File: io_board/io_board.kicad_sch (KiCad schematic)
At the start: 83 parts, among them J10 RST1, J11 D1, J12 Osc2, J13 Rung2, J14 Sin2, J15 Gate2, J16 Ring, J18 RST2, J19 D2, J21 CV1, J22 CV2, J4 STRB1, J5 STRB2, J6 Osc1, J7 Sin1, J8 Rung1, J9 Gate1, Q1 2N3904, Q10 2N3904, Q11 2N3904, Q2 2N3904, Q5 2N3904, Q6 2N3904, Q7 2N3904, Q8 2N3904, Q9 2N3904, SW1 SW_SPDT, U3 TL074

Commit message: Routing done, panel done
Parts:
- U3: value TL074 -> (none); footprint Package_DIP:DIP-14_W7.62mm_Socket_LongPads -> (none)
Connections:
- net Clk2: now also J20.7 (Pin_7); no longer J20.8 (Pin_8)
- net D1: now also J17.5 (Pin_5); no longer J17.4 (Pin_4)
- net Osc1: now also J17.6 (Pin_6); no longer J17.7 (Pin_7)
- net Osc2: now also J20.5 (Pin_5); no longer J20.7 (Pin_7)
- net Osc3sw: now also J20.3 (Pin_3); no longer J20.5 (Pin_5)
- net QB8: now also J20.8 (Pin_8); no longer J20.9 (Pin_9)
- net RM: now also J17.4 (Pin_4); no longer J17.6 (Pin_6)
- net Rst1: now also J17.7 (Pin_7); no longer J17.3 (Pin_3)
- net Rst2: now also J20.9 (Pin_9); no longer J20.3 (Pin_3)
- net Rung2: now also J20.10 (Pin_10); no longer J20.11 (Pin_11)
- net Sin2: now also J20.11 (Pin_11); no longer J20.10 (Pin_10)
- net at R57.1, R59.1: now also U3.12 (+); no longer U3.10 (+)
- net at D9.2 (A): now also U3.14; no longer U3.8
- net at R58.1: now also U3.10 (+); no longer U3.12 (+)
- net at R54.2, R55.1: now also U3.13 (-), U3.9 (-); no longer U3.13 (-), U3.9 (-)
- net at D10.2 (A): now also U3.8; no longer U3.14

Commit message: Updates to panel etc.
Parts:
- added R72, R74: 100k, Resistor_THT:R_Axial_DIN0204_L3.6mm_D1.6mm_P7.62mm_Horizontal, symbol Device:R
- added R73, R75: 22k, Resistor_THT:R_Axial_DIN0204_L3.6mm_D1.6mm_P7.62mm_Horizontal, symbol Device:R
- U3: value (none) -> TL074; footprint (none) -> Package_DIP:DIP-14_W7.62mm_Socket_LongPads
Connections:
- net +12V: now also R72.1, R74.1
- net GND: now also R73.2, R75.2
- net at J22.TN: now also R74.2, R75.1
- net at J21.TN: now also R72.2, R73.1

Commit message: Added negative CV protection diodes
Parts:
- added D13, D14, D15, D16: (no value), symbol Diode:BAT42
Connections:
- net CV1: now also D15.1 (K)
- net CV2: now also D16.1 (K)
- net GND: now also D13.2 (A), D14.2 (A), D15.2 (A), D16.2 (A)
- net at Q8.2 (B), R40.2: now also D14.1 (K)
- net at Q7.2 (B), R39.2: now also D13.1 (K)
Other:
- moved on the sheet: CVR2, FREQ2, J22, R63, R64, R71, R74, R75, TH3, TH4

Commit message: Flip flop on CV protection diodes
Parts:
- removed D15, D16: (no value), symbol Diode:BAT42
- D13, D14: value (none) -> BAT42; footprint (none) -> Diode_THT:D_DO-35_SOD27_P7.62mm_Horizontal
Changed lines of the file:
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@@
   (junction (at 317.5 64.77) (diameter 0) (color 0 0 0 0)
   )
-  (junction (at 323.85 64.77) (diameter 0) (color 0 0 0 0)
-  )
   (junction (at 387.35 64.77) (diameter 0) (color 0 0 0 0)
   )
@@
   (junction (at 125.73 43.18) (diameter 0) (color 0 0 0 0)
   )
-  (junction (at 393.065 64.77) (diameter 0) (color 0 0 0 0)
-  )
   (junction (at 219.71 43.18) (diameter 0) (color 0 0 0 0)
   )
@@
     (stroke (width 0) (type default) (color 0 0 0 0))
   )
-  (wire (pts (xy 323.85 64.77) (xy 327.66 64.77))
-    (stroke (width 0) (type default) (color 0 0 0 0))
-  )
   (polyline (pts (xy 15.24 251.46) (xy 15.24 157.48))
     (stroke (width 0) (type default) (color 0 0 0 0))
@@
     (stroke (width 0) (type default) (color 0 0 0 0))
   )
-  (wire (pts (xy 393.065 64.77) (xy 396.24 64.77))
-    (stroke (width 0) (type default) (color 0 0 0 0))
-  )
   (wire (pts (xy 76.2 138.43) (xy 76.2 139.7))
     (stroke (width 0) (type default) (color 0 0 0 0))
@@
     (stroke (width 0) (type default) (color 0 0 0 0))
   )
-  (wire (pts (xy 323.85 64.77) (xy 323.85 67.945))
-    (stroke (width 0) (type default) (color 0 0 0 0))
-  )
   (wire (pts (xy 167.64 201.93) (xy 170.18 201.93))
     (stroke (width 0) (type default) (color 0 0 0 0))
@@
     (stroke (width 0) (type default) (color 0 0 0 0))
   )
-  (wire (pts (xy 393.065 64.77) (xy 393.065 67.945))
-    (stroke (width 0) (type default) (color 0 0 0 0))
-  )
   (wire (pts (xy 110.49 231.14) (xy 110.49 232.41))
     (stroke (width 0) (type default) (color 0 0 0 0))
@@
     (stroke (width 0) (type default) (color 0 0 0 0))
   )
-  (wire (pts (xy 317.5 64.77) (xy 323.85 64.77))
+  (wire (pts (xy 317.5 64.77) (xy 327.66 64.77))
     (stroke (width 0) (type default) (color 0 0 0 0))
   )
@@
     (stroke (width 0) (type default) (color 0 0 0 0))
   )
-  (wire (pts (xy 393.065 75.565) (xy 393.065 79.375))
-    (stroke (width 0) (type default) (color 0 0 0 0))
-  )
   (wire (pts (xy 40.64 240.03) (xy 40.64 242.57))
     (stroke (width 0) (type default) (color 0 0 0 0))
@@
     (stroke (width 0) (type default) (color 0 0 0 0))
   )
-  (wire (pts (xy 323.85 75.565) (xy 323.85 79.375))
-    (stroke (width 0) (type default) (color 0 0 0 0))
-  )
   (wire (pts (xy 135.89 67.31) (xy 135.89 48.26))
     (stroke (width 0) (type default) (color 0 0 0 0))
@@
     (stroke (width 0) (type default) (color 0 0 0 0))
   )
-  (wire (pts (xy 387.35 64.77) (xy 393.065 64.77))
+  (wire (pts (xy 387.35 64.77) (xy 396.24 64.77))
     (stroke (width 0) (type default) (color 0 0 0 0))
   )
@@
       (effects (font (size 1.27 1.27)) hide)
     )
-    (property "Value" "" (id 1) (at 46.99 104.14 0))
+    (property "Value" "GND" (id 1) (at 46.99 104.14 0))
     (property "Footprint" "" (id 2) (at 46.99 99.06 0)
       (effects (font (size 1.27 1.27)) hide)
@@
       (effects (font (size 1.27 1.27)) (justify left))
     )
-    (property "Value" "" (id 1) (at 39.37 95.25 90)
+    (property "Value" "BAT42" (id 1) (at 39.37 95.25 90)
       (effects (font (size 1.27 1.27)) (justify left))
     )
-    (property "Footprint" "" (id 2) (at 42.545 93.98 0)
+    (property "Footprint" "Diode_THT:D_DO-35_SOD27_P7.62mm_Horizontal" (id 2) (at 42.545 93.98 0)
       (effects (font (size 1.27 1.27)) hide)
     )
@@
       (effects (font (size 1.27 1.27)) hide)
     )
-    (property "Value" "" (id 1) (at 46.99 64.77 0))
+    (property "Value" "GND" (id 1) (at 46.99 64.77 0))
     (property "Footprint" "" (id 2) (at 46.99 59.69 0)
       (effects (font (size 1.27 1.27)) hide)
@@
     (pin "TN")
   )
-  (symbol (lib_id "power:GND") (at 393.065 79.375 0) (unit 1)
-    (in_bom yes) (on_board yes) (fields_autoplaced)
-    (property "Reference" "#PWR097" (id 0) (at 393.065 85.725 0)
-      (effects (font (size 1.27 1.27)) hide)
-    )
-    (property "Value" "" (id 1) (at 393.065 84.455 0))
-    (property "Footprint" "" (id 2) (at 393.065 79.375 0)
-      (effects (font (size 1.27 1.27)) hide)
-    )
-    (property "Datasheet" "" (id 3) (at 393.065 79.375 0)
-      (effects (font (size 1.27 1.27)) hide)
-    )
-    (pin "1")
-  )
   (symbol (lib_id "power:-12V") (at 177.8 156.21 180) (unit 1)
     (in_bom yes) (on_board yes) (fields_autoplaced)
@@
     (pin "3")
   )
-  (symbol (lib_id "Diode:BAT42") (at 393.065 71.755 270) (unit 1)
-    (in_bom yes) (on_board yes) (fields_autoplaced)
-    (property "Reference" "D16" (id 0) (at 395.605 70.1674 90)
-      (effects (font (size 1.27 1.27)) (justify left))
-    )
-    (property "Value" "" (id 1) (at 395.605 72.7074 90)
-      (effects (font (size 1.27 1.27)) (justify left))
-    )
-    (property "Footprint" "" (id 2) (at 388.62 71.755 0)
-      (effects (font (size 1.27 1.27)) hide)
-    )
-    (property "Datasheet" "http://www.vishay.com/docs/85660/bat42.pdf" (id 3) (at 393.065 71.755 0)
-      (effects (font (size 1.27 1.27)) hide)
-    )
-    (pin "1")
-    (pin "2")
-  )
   (symbol (lib_id "Device:R") (at 212.09 201.93 270) (unit 1)
     (in_bom yes) (on_board yes) (fields_autoplaced)
@@
     (pin "2")
   )
-  (symbol (lib_id "Diode:BAT42") (at 323.85 71.755 270) (unit 1)
-    (in_bom yes) (on_board yes) (fields_autoplaced)
-    (property "Reference" "D15" (id 0) (at 326.39 70.1674 90)
-      (effects (font (size 1.27 1.27)) (justify left))
-    )
-    (property "Value" "" (id 1) (at 326.39 72.7074 90)
-      (effects (font (size 1.27 1.27)) (justify left))
-    )
-    (property "Footprint" "" (id 2) (at 319.405 71.755 0)
-      (effects (font (size 1.27 1.27)) hide)
-    )
-    (property "Datasheet" "http://www.vishay.com/docs/85660/bat42.pdf" (id 3) (at 323.85 71.755 0)
-      (effects (font (size 1.27 1.27)) hide)
-    )
-    (pin "1")
-    (pin "2")
-  )
   (symbol (lib_id "Device:R") (at 55.88 54.61 180) (unit 1)
     (in_bom yes) (on_board yes) (fields_autoplaced)
@@
     (pin "2")
   )
-  (symbol (lib_id "power:GND") (at 323.85 79.375 0) (unit 1)
-    (in_bom yes) (on_board yes) (fields_autoplaced)
-    (property "Reference" "#PWR093" (id 0) (at 323.85 85.725 0)
-      (effects (font (size 1.27 1.27)) hide)
-    )
-    (property "Value" "" (id 1) (at 323.85 84.455 0))
-    (property "Footprint" "" (id 2) (at 323.85 79.375 0)
-      (effects (font (size 1.27 1.27)) hide)
-    )
-    (property "Datasheet" "" (id 3) (at 323.85 79.375 0)
-      (effects (font (size 1.27 1.27)) hide)
-    )
-    (pin "1")
-  )
   (symbol (lib_id "Device:R") (at 36.83 196.85 90) (unit 1)
     (in_bom yes) (on_board yes)
@@
       (effects (font (size 1.27 1.27)) (justify left))
     )
-    (property "Value" "" (id 1) (at 39.37 55.88 90)
+    (property "Value" "BAT42" (id 1) (at 39.37 55.88 90)
       (effects (font (size 1.27 1.27)) (justify left))
     )
-    (property "Footprint" "" (id 2) (at 42.545 54.61 0)
+    (property "Footprint" "Diode_THT:D_DO-35_SOD27_P7.62mm_Horizontal" (id 2) (at 42.545 54.61 0)
       (effects (font (size 1.27 1.27)) hide)
     )
@@
       (reference "#PWR092") (unit 1) (value "GND") (footprint "")
     )
-    (path "/c6c801eb-a62e-4709-ba8f-cc4ab2962bb0"
-      (reference "#PWR093") (unit 1) (value "GND") (footprint "")
-    )
-    (path "/5b01a551-5830-4c34-991f-8c4bd9fdd15c"
-      (reference "#PWR097") (unit 1) (value "GND") (footprint "")
-    )
     (path "/5e4d8429-e4c9-42f2-9cfd-97a2e6b0fe00"
       (reference "#PWR0101") (unit 1) (value "GND") (footprint "")
@@
       (reference "D14") (unit 1) (value "BAT42") (footprint "Diode_THT:D_DO-35_SOD27_P7.62mm_Horizontal")
     )
-    (path "/b4e0d83a-1e44-4055-b69b-34a66bed64e8"
-      (reference "D15") (unit 1) (value "BAT42") (footprint "Diode_THT:D_DO-35_SOD27_P7.62mm_Horizontal")
-    )
-    (path "/61cd796f-f9d1-45f6-922e-b46b67f716a1"
-      (reference "D16") (unit 1) (value "BAT42") (footprint "Diode_THT:D_DO-35_SOD27_P7.62mm_Horizontal")
-    )
     (path "/a2167960-f9c9-4609-b610-0da799bcc1d1"

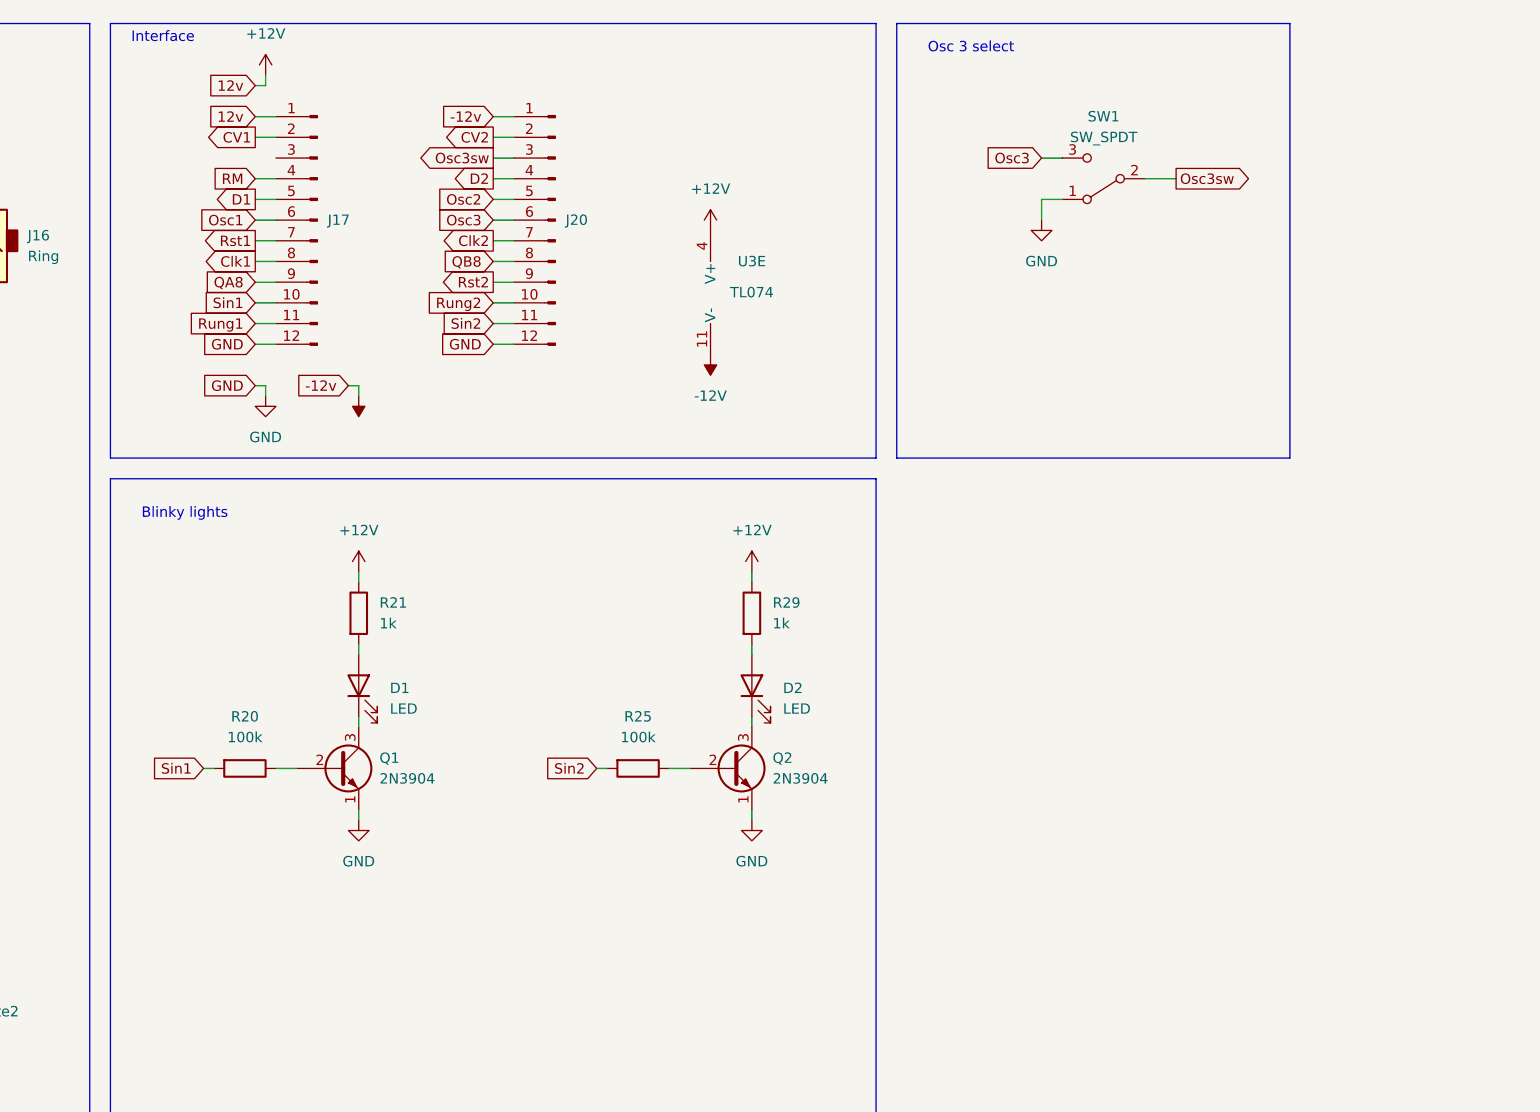
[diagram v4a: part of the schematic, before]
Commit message: Added range switch
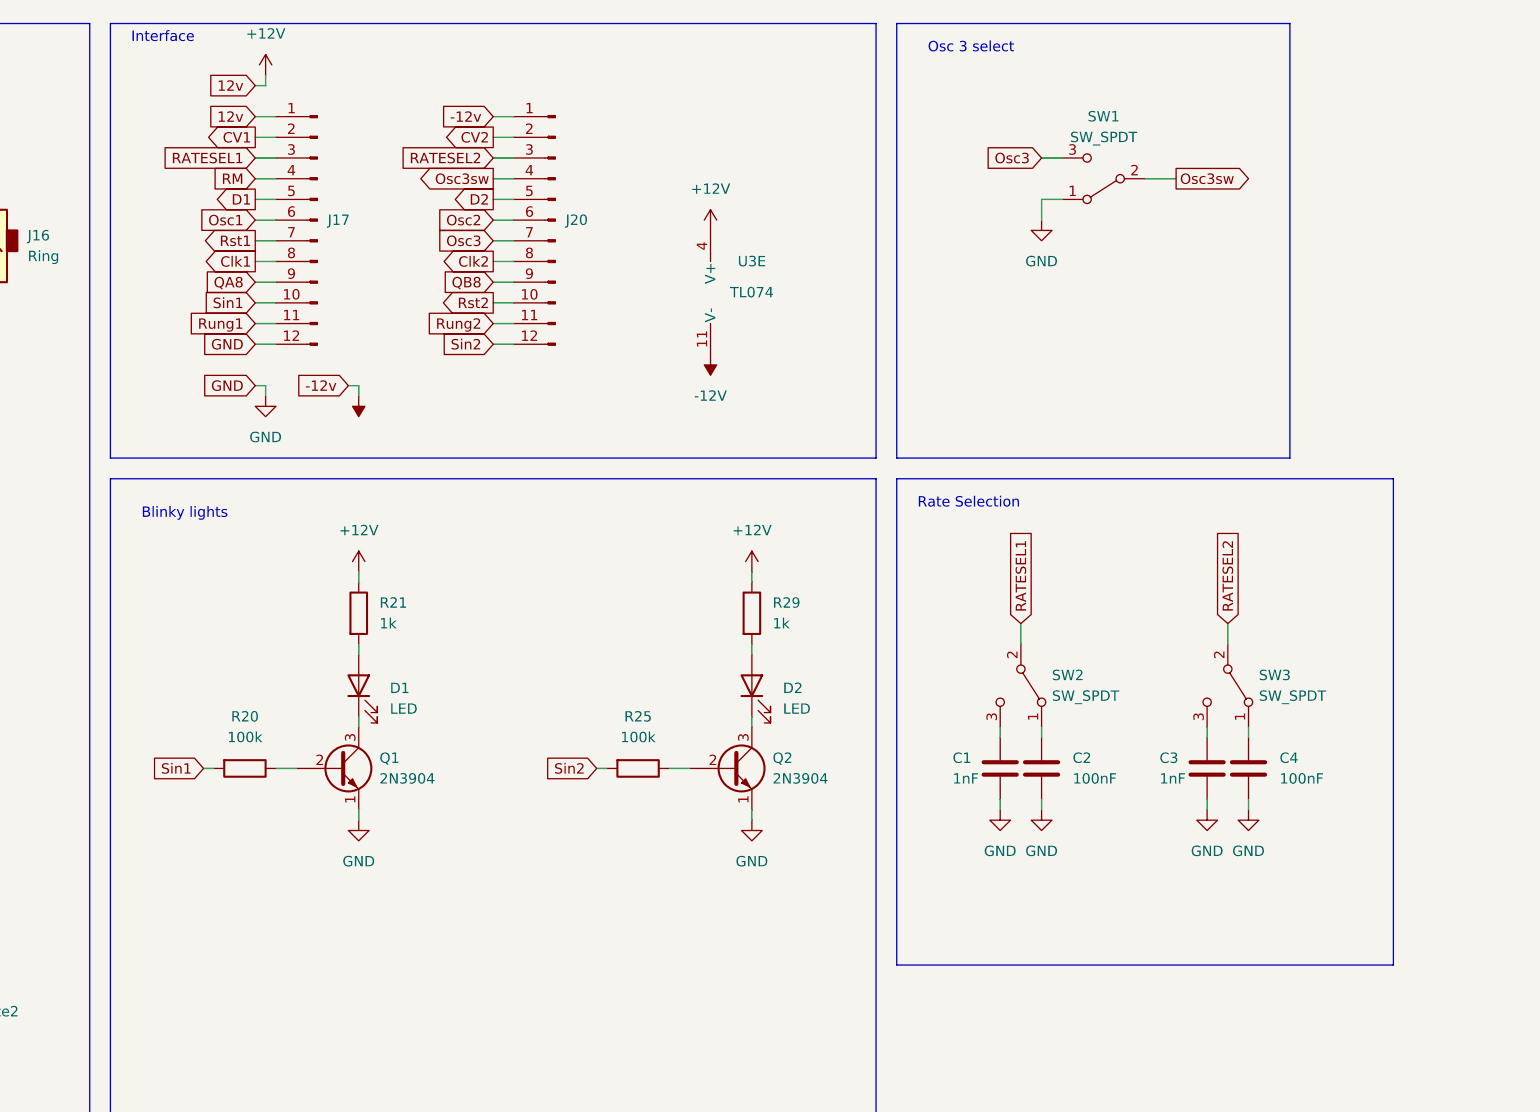
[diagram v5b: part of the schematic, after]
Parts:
- added C1, C3: 1nF, Capacitor_THT:C_Disc_D5.0mm_W2.5mm_P2.50mm, symbol Device:C
- added C2, C4: 100nF, Capacitor_THT:C_Disc_D5.0mm_W2.5mm_P2.50mm, symbol Device:C
- added SW2, SW3: SW_SPDT, winterbloom:Miniature_Switch_SPDT_2.54MM, symbol Switch:SW_SPDT
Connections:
- net Clk2: now also J20.8 (Pin_8); no longer J20.7 (Pin_7)
- net D2: now also J20.5 (Pin_5); no longer J20.4 (Pin_4)
- net GND: now also C1.2, C2.2, C3.2, C4.2; no longer J20.12 (Pin_12)
- net Osc2: now also J20.6 (Pin_6); no longer J20.5 (Pin_5)
- net Osc3: now also J20.7 (Pin_7); no longer J20.6 (Pin_6)
- net Osc3sw: now also J20.4 (Pin_4); no longer J20.3 (Pin_3)
- net QB8: now also J20.9 (Pin_9); no longer J20.8 (Pin_8)
- net Rst2: now also J20.10 (Pin_10); no longer J20.9 (Pin_9)
- net Rung2: now also J20.11 (Pin_11); no longer J20.10 (Pin_10)
- net Sin2: now also J20.12 (Pin_12); no longer J20.11 (Pin_11)
- net RATESEL1: now reaches J17.3 (Pin_3)
- net RATESEL1: now also SW2.2 (B)
- new net: C3.1, SW3.3 (C)
- new net: C4.1, SW3.1 (A)
- new net: C1.1, SW2.3 (C)
- new net: C2.1, SW2.1 (A)
- new net RATESEL2: J20.3 (Pin_3), SW3.2 (B)
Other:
- note added: "Rate Selection"
